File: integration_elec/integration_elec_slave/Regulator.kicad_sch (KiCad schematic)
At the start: 24 parts, among them U4 TPS54335ADDAR

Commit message: EM - fuck it we merge et on cree deux branches
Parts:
- renumbered C36 to C20, C40 to C21, C42 to C22, C44 to C23, C45 to C24, C46 to C25, C60 to C26, C61 to C27, C62 to C28, C63 to C29, C64 to C30, C65 to C31, D9 to D2, L4 to L2, R43 to R14, R44 to R15, R45 to R16, R46 to R17, R47 to R18, R54 to R19, R44 to R20, TP2 to TP1, TP1 to TP2
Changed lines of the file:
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@@
 		(on_board yes)
 		(dnp no)
-		(property "Reference" "R47"
+		(property "Reference" "R18"
 			(at 115.062 44.45 0)
 			(effects
@@
 			(project "integration_elec_slave"
 				(path "/f8f45849-17b1-4cdb-b0ac-47b1208e44f3/408e7880-979e-40de-9541-c2200e8ca76c"
-					(reference "R47")
+					(reference "R18")
 					(unit 1)
 				)
@@
 		(on_board yes)
 		(dnp no)
-		(property "Reference" "C44"
+		(property "Reference" "C23"
 			(at 43.815 34.925 0)
 			(effects
@@
 			(project "integration_elec_slave"
 				(path "/f8f45849-17b1-4cdb-b0ac-47b1208e44f3/408e7880-979e-40de-9541-c2200e8ca76c"
-					(reference "C44")
+					(reference "C23")
 					(unit 1)
 				)
@@
 		(on_board yes)
 		(dnp no)
-		(property "Reference" "D9"
+		(property "Reference" "D2"
 			(at 153.67 47.625 90)
 			(effects
@@
 			(project "integration_elec_slave"
 				(path "/f8f45849-17b1-4cdb-b0ac-47b1208e44f3/408e7880-979e-40de-9541-c2200e8ca76c"
-					(reference "D9")
+					(reference "D2")
 					(unit 1)
 				)
@@
 		(on_board yes)
 		(dnp no)
-		(property "Reference" "TP2"
+		(property "Reference" "TP1"
 			(at 78.5368 69.723 0)
 			(effects
@@
 			(project "integration_elec_slave"
 				(path "/f8f45849-17b1-4cdb-b0ac-47b1208e44f3/408e7880-979e-40de-9541-c2200e8ca76c"
-					(reference "TP2")
+					(reference "TP1")
 					(unit 1)
 				)
@@
 		(on_board yes)
 		(dnp no)
-		(property "Reference" "R45"
+		(property "Reference" "R16"
 			(at 50.165 48.895 0)
 			(effects
@@
 			(project "integration_elec_slave"
 				(path "/f8f45849-17b1-4cdb-b0ac-47b1208e44f3/408e7880-979e-40de-9541-c2200e8ca76c"
-					(reference "R45")
+					(reference "R16")
 					(unit 1)
 				)
@@
 		(on_board yes)
 		(dnp no)
-		(property "Reference" "C36"
+		(property "Reference" "C20"
 			(at 30.48 34.925 0)
 			(effects
@@
 			(project "integration_elec_slave"
 				(path "/f8f45849-17b1-4cdb-b0ac-47b1208e44f3/408e7880-979e-40de-9541-c2200e8ca76c"
-					(reference "C36")
+					(reference "C20")
 					(unit 1)
 				)
@@
 		(on_board yes)
 		(dnp no)
-		(property "Reference" "C63"
+		(property "Reference" "C29"
 			(at 128.27 48.895 0)
 			(effects
@@
 			(project "integration_elec_slave"
 				(path "/f8f45849-17b1-4cdb-b0ac-47b1208e44f3/408e7880-979e-40de-9541-c2200e8ca76c"
-					(reference "C63")
+					(reference "C29")
 					(unit 1)
 				)
@@
 		(dnp no)
 		(fields_autoplaced yes)
-		(property "Reference" "TP1"
+		(property "Reference" "TP2"
 			(at 142.24 30.9879 0)
 			(effects
@@
 			(project ""
 				(path "/f8f45849-17b1-4cdb-b0ac-47b1208e44f3/408e7880-979e-40de-9541-c2200e8ca76c"
-					(reference "TP1")
+					(reference "TP2")
 					(unit 1)
 				)
@@
 		(on_board yes)
 		(dnp no)
-		(property "Reference" "R54"
+		(property "Reference" "R19"
 			(at 115.062 54.61 0)
 			(effects
@@
 			(project "integration_elec_slave"
 				(path "/f8f45849-17b1-4cdb-b0ac-47b1208e44f3/408e7880-979e-40de-9541-c2200e8ca76c"
-					(reference "R54")
+					(reference "R19")
 					(unit 1)
 				)
@@
 		(on_board yes)
 		(dnp no)
-		(property "Reference" "C62"
+		(property "Reference" "C28"
 			(at 121.92 48.895 0)
 			(effects
@@
 			(project "integration_elec_slave"
 				(path "/f8f45849-17b1-4cdb-b0ac-47b1208e44f3/408e7880-979e-40de-9541-c2200e8ca76c"
-					(reference "C62")
+					(reference "C28")
 					(unit 1)
 				)
@@
 		(on_board yes)
 		(dnp no)
-		(property "Reference" "C42"
+		(property "Reference" "C22"
 			(at 39.37 34.925 0)
 			(effects
@@
 			(project "integration_elec_slave"
 				(path "/f8f45849-17b1-4cdb-b0ac-47b1208e44f3/408e7880-979e-40de-9541-c2200e8ca76c"
-					(reference "C42")
+					(reference "C22")
 					(unit 1)
 				)
@@
 		(on_board yes)
 		(dnp no)
-		(property "Reference" "C40"
+		(property "Reference" "C21"
 			(at 34.29 34.925 0)
 			(effects
@@
 			(project "integration_elec_slave"
 				(path "/f8f45849-17b1-4cdb-b0ac-47b1208e44f3/408e7880-979e-40de-9541-c2200e8ca76c"
-					(reference "C40")
+					(reference "C21")
 					(unit 1)
 				)
@@
 		(on_board yes)
 		(dnp no)
-		(property "Reference" "R44"
+		(property "Reference" "R15"
 			(at 43.815 48.895 0)
 			(effects
@@
 			(project "integration_elec_slave"
 				(path "/f8f45849-17b1-4cdb-b0ac-47b1208e44f3/408e7880-979e-40de-9541-c2200e8ca76c"
-					(reference "R44")
+					(reference "R15")
 					(unit 1)
 				)
@@
 		(on_board yes)
 		(dnp no)
-		(property "Reference" "C64"
+		(property "Reference" "C30"
 			(at 134.62 48.895 0)
 			(effects
@@
 			(project "integration_elec_slave"
 				(path "/f8f45849-17b1-4cdb-b0ac-47b1208e44f3/408e7880-979e-40de-9541-c2200e8ca76c"
-					(reference "C64")
+					(reference "C30")
 					(unit 1)
 				)
@@
 		(on_board yes)
 		(dnp no)
-		(property "Reference" "C65"
+		(property "Reference" "C31"
 			(at 141.605 48.895 0)
 			(effects
@@
 			(project "integration_elec_slave"
 				(path "/f8f45849-17b1-4cdb-b0ac-47b1208e44f3/408e7880-979e-40de-9541-c2200e8ca76c"
-					(reference "C65")
+					(reference "C31")
 					(unit 1)
 				)
@@
 		(on_board yes)
 		(dnp no)
-		(property "Reference" "C45"
+		(property "Reference" "C24"
 			(at 48.641 58.801 0)
 			(effects
@@
 			(project "integration_elec_slave"
 				(path "/f8f45849-17b1-4cdb-b0ac-47b1208e44f3/408e7880-979e-40de-9541-c2200e8ca76c"
-					(reference "C45")
+					(reference "C24")
 					(unit 1)
 				)
@@
 		(dnp no)
 		(fields_autoplaced yes)
-		(property "Reference" "L4"
+		(property "Reference" "L2"
 			(at 102.87 36.83 0)
 			(effects
@@
 			(project "integration_elec_slave"
 				(path "/f8f45849-17b1-4cdb-b0ac-47b1208e44f3/408e7880-979e-40de-9541-c2200e8ca76c"
-					(reference "L4")
+					(reference "L2")
 					(unit 1)
 				)
@@
 		(on_board yes)
 		(dnp no)
-		(property "Reference" "C46"
+		(property "Reference" "C25"
 			(at 60.325 55.245 0)
 			(effects
@@
 			(project "integration_elec_slave"
 				(path "/f8f45849-17b1-4cdb-b0ac-47b1208e44f3/408e7880-979e-40de-9541-c2200e8ca76c"
-					(reference "C46")
+					(reference "C25")
 					(unit 1)
 				)
@@
 		(on_board yes)
 		(dnp no)
-		(property "Reference" "R43"
+		(property "Reference" "R14"
 			(at 50.165 39.37 0)
 			(effects
@@
 			(project "integration_elec_slave"
 				(path "/f8f45849-17b1-4cdb-b0ac-47b1208e44f3/408e7880-979e-40de-9541-c2200e8ca76c"
-					(reference "R43")
+					(reference "R14")
 					(unit 1)
 				)
@@
 		(on_board yes)
 		(dnp no)
-		(property "Reference" "#PWR065"
+		(property "Reference" "#PWR029"
 			(at 69.85 71.755 0)
 			(effects
@@
 			(project "integration_elec_slave"
 				(path "/f8f45849-17b1-4cdb-b0ac-47b1208e44f3/408e7880-979e-40de-9541-c2200e8ca76c"
-					(reference "#PWR065")
+					(reference "#PWR029")
 					(unit 1)
 				)
@@
 		(on_board yes)
 		(dnp no)
-		(property "Reference" "R44"
+		(property "Reference" "R20"
 			(at 152.4 57.785 0)
 			(effects
@@
 			(project "integration_elec_slave"
 				(path "/f8f45849-17b1-4cdb-b0ac-47b1208e44f3/408e7880-979e-40de-9541-c2200e8ca76c"
-					(reference "R44")
+					(reference "R20")
 					(unit 1)
 				)
@@
 		(on_board yes)
 		(dnp no)
-		(property "Reference" "C61"
+		(property "Reference" "C27"
 			(at 116.205 48.895 0)
 			(effects
@@
 			(project "integration_elec_slave"
 				(path "/f8f45849-17b1-4cdb-b0ac-47b1208e44f3/408e7880-979e-40de-9541-c2200e8ca76c"
-					(reference "C61")
+					(reference "C27")
 					(unit 1)
 				)
@@
 		(on_board yes)
 		(dnp no)
-		(property "Reference" "R46"
+		(property "Reference" "R17"
 			(at 60.325 50.8 0)
 			(effects
@@
 			(project "integration_elec_slave"
 				(path "/f8f45849-17b1-4cdb-b0ac-47b1208e44f3/408e7880-979e-40de-9541-c2200e8ca76c"
-					(reference "R46")
+					(reference "R17")
 					(unit 1)
 				)
@@
 		(dnp no)
 		(fields_autoplaced yes)
-		(property "Reference" "#PWR019"
+		(property "Reference" "#PWR031"
 			(at 160.02 44.45 0)
 			(effects
@@
 			(project ""
 				(path "/f8f45849-17b1-4cdb-b0ac-47b1208e44f3/408e7880-979e-40de-9541-c2200e8ca76c"
-					(reference "#PWR019")
+					(reference "#PWR031")
 					(unit 1)
 				)
@@
 		(on_board yes)
 		(dnp no)
-		(property "Reference" "#PWR075"
+		(property "Reference" "#PWR030"
 			(at 149.86 70.485 0)
 			(effects
@@
 			(project "integration_elec_slave"
 				(path "/f8f45849-17b1-4cdb-b0ac-47b1208e44f3/408e7880-979e-40de-9541-c2200e8ca76c"
-					(reference "#PWR075")
+					(reference "#PWR030")
 					(unit 1)
 				)
@@
 		(on_board yes)
 		(dnp no)
-		(property "Reference" "C60"
+		(property "Reference" "C26"
 			(at 90.805 33.655 90)
 			(effects
@@
 			(project "integration_elec_slave"
 				(path "/f8f45849-17b1-4cdb-b0ac-47b1208e44f3/408e7880-979e-40de-9541-c2200e8ca76c"
-					(reference "C60")
+					(reference "C26")
 					(unit 1)
 				)
@@
 		(dnp no)
 		(fields_autoplaced yes)
-		(property "Reference" "#PWR020"
+		(property "Reference" "#PWR028"
 			(at 20.32 36.83 0)
 			(effects
@@
 			(project ""
 				(path "/f8f45849-17b1-4cdb-b0ac-47b1208e44f3/408e7880-979e-40de-9541-c2200e8ca76c"
-					(reference "#PWR020")
-					(unit 1)
-				)
+					(reference "#PWR028")
+					(unit 1)
+				)

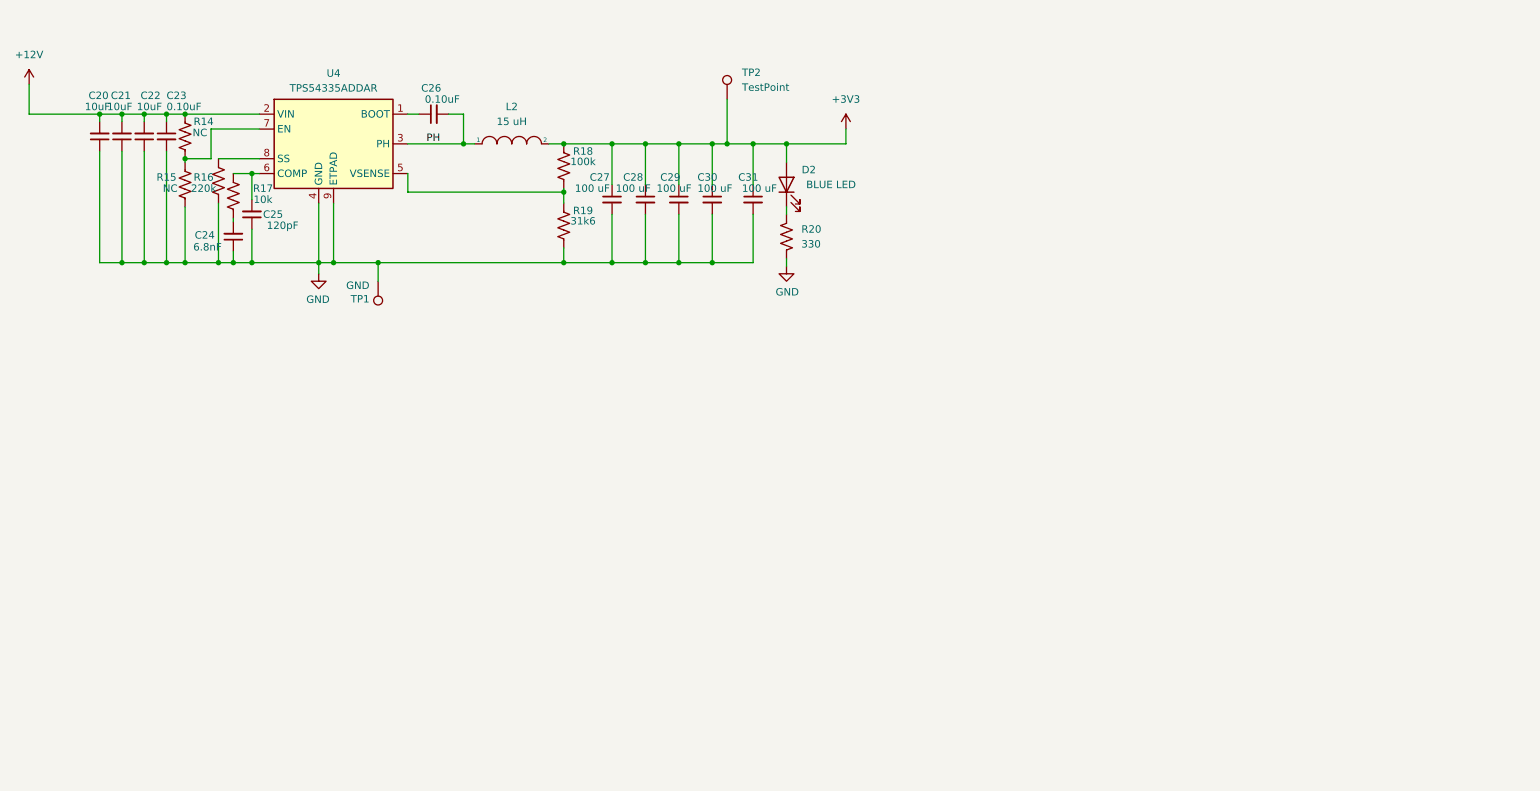
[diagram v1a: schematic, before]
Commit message: EM - Correction des bus
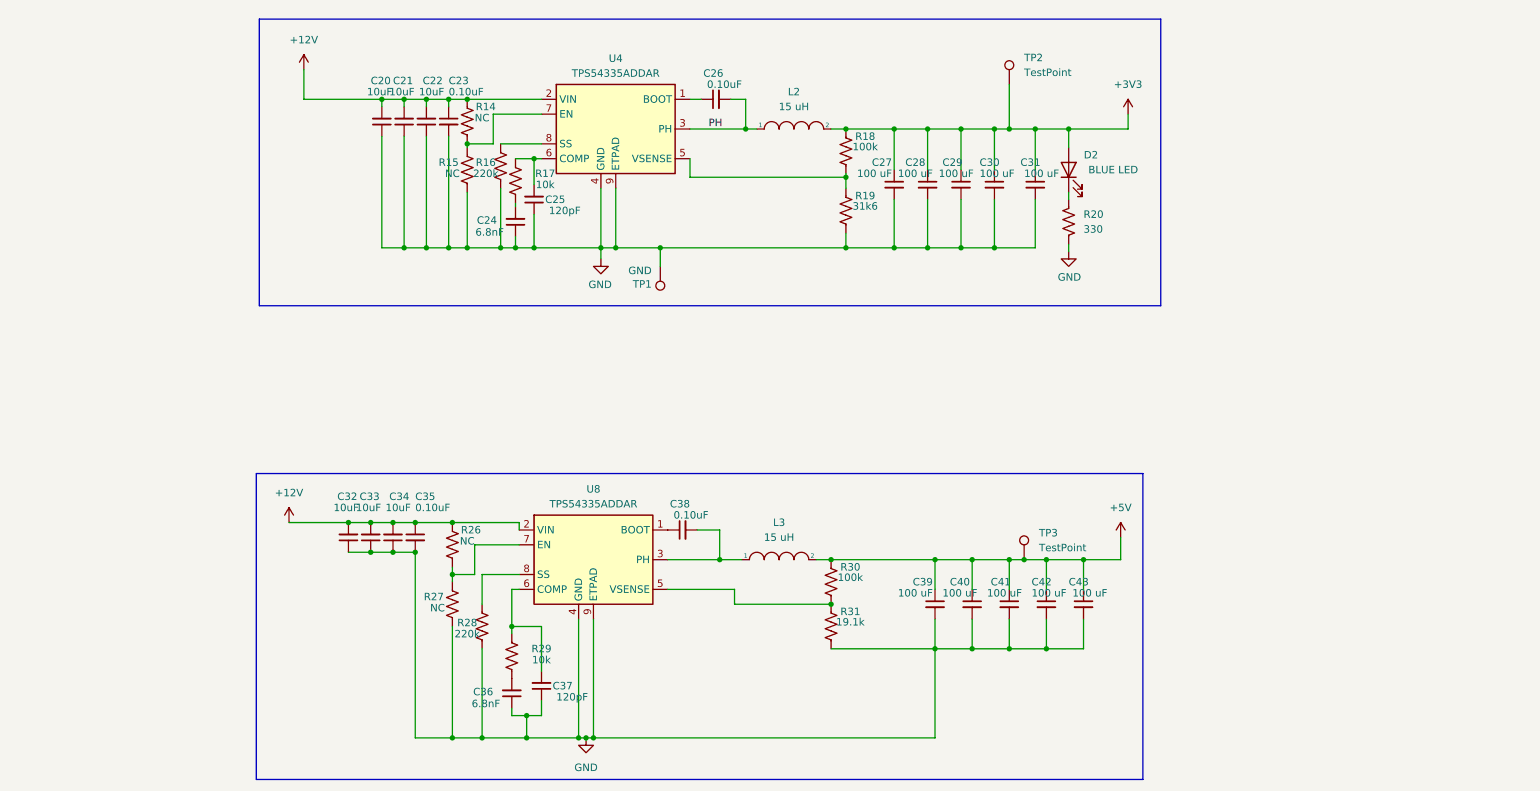
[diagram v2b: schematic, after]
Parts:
- added C32, C33, C34: 10uF, Capacitor_SMD:C_0805_2012Metric_Pad1.18x1.45mm_HandSolder, symbol Device:C_Small
- added C35, C38: 0.10uF, Capacitor_SMD:C_0805_2012Metric_Pad1.18x1.45mm_HandSolder, symbol Device:C_Small
- added C36: 6.8nF, Capacitor_SMD:C_0805_2012Metric_Pad1.18x1.45mm_HandSolder, symbol Device:C_Small
- added C37: 120pF, Capacitor_SMD:C_0805_2012Metric_Pad1.18x1.45mm_HandSolder, symbol Device:C_Small
- added C39, C40, C41, C42, C43: 100 uF, Capacitor_SMD:C_1206_3216Metric, symbol Device:C_Small
- added L3: 15 uH, Inductors:IND_BOURNS_SRR1280, symbol pspice:INDUCTOR
- added R26, R27: NC, Resistor_SMD:R_0805_2012Metric_Pad1.20x1.40mm_HandSolder, symbol Device:R_US
- added R28: 220k, Resistor_SMD:R_0805_2012Metric_Pad1.20x1.40mm_HandSolder, symbol Device:R_US
- added R29: 10k, Resistor_SMD:R_0805_2012Metric_Pad1.20x1.40mm_HandSolder, symbol Device:R_US
- added R30: 100k, Resistor_SMD:R_0805_2012Metric_Pad1.20x1.40mm_HandSolder, symbol Device:R_US
- added R31: 19.1k, Resistor_SMD:R_0805_2012Metric_Pad1.20x1.40mm_HandSolder, symbol Device:R_US
- added TP3: TestPoint, symbol Connector:TestPoint
- added U8: TPS54335ADDAR, Package_SO:TI_SO-PowerPAD-8_ThermalVias, symbol Regulator_Switching:TPS54336ADDA
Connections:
- net +12V: now also C32.2, C33.2, C34.2, C35.1, R26.1, U8.2 (VIN)
- net GND: now also C32.1, C33.1, C34.1, C35.2, C36.1, C37.1, C39.2, C40.2, C41.2, C42.2, C43.2, R27.2, R28.2, R31.2, U8.4 (GND), U8.9 (ETPAD)
- new net: R26.2, R27.1, U8.7 (EN)
- new net: R28.1, U8.8 (SS)
- new net: C38.2, L3.1, U8.3 (PH)
- new net: C37.2, R29.1, U8.6 (COMP)
- new net: C36.2, R29.2
- new net: C38.1, U8.1 (BOOT)
- new net: R30.2, R31.1, U8.5 (VSENSE)
- new net +5V: C39.1, C40.1, C41.1, C42.1, C43.1, L3.2, R30.1, TP3.1
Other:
- moved on the sheet: C20, C21, C22, C23, C24, C25, C26, C27, C28, C29, C30, C31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

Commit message: EM - Fini schématique attente de review
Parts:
- R31: DigiKey (none) -> 311-19.1KCRCT-ND
- TP2, TP3: footprint (none) -> TestPoint:TestPoint_Plated_Hole_D2.0mm
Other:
- moved on the sheet: C24, R16

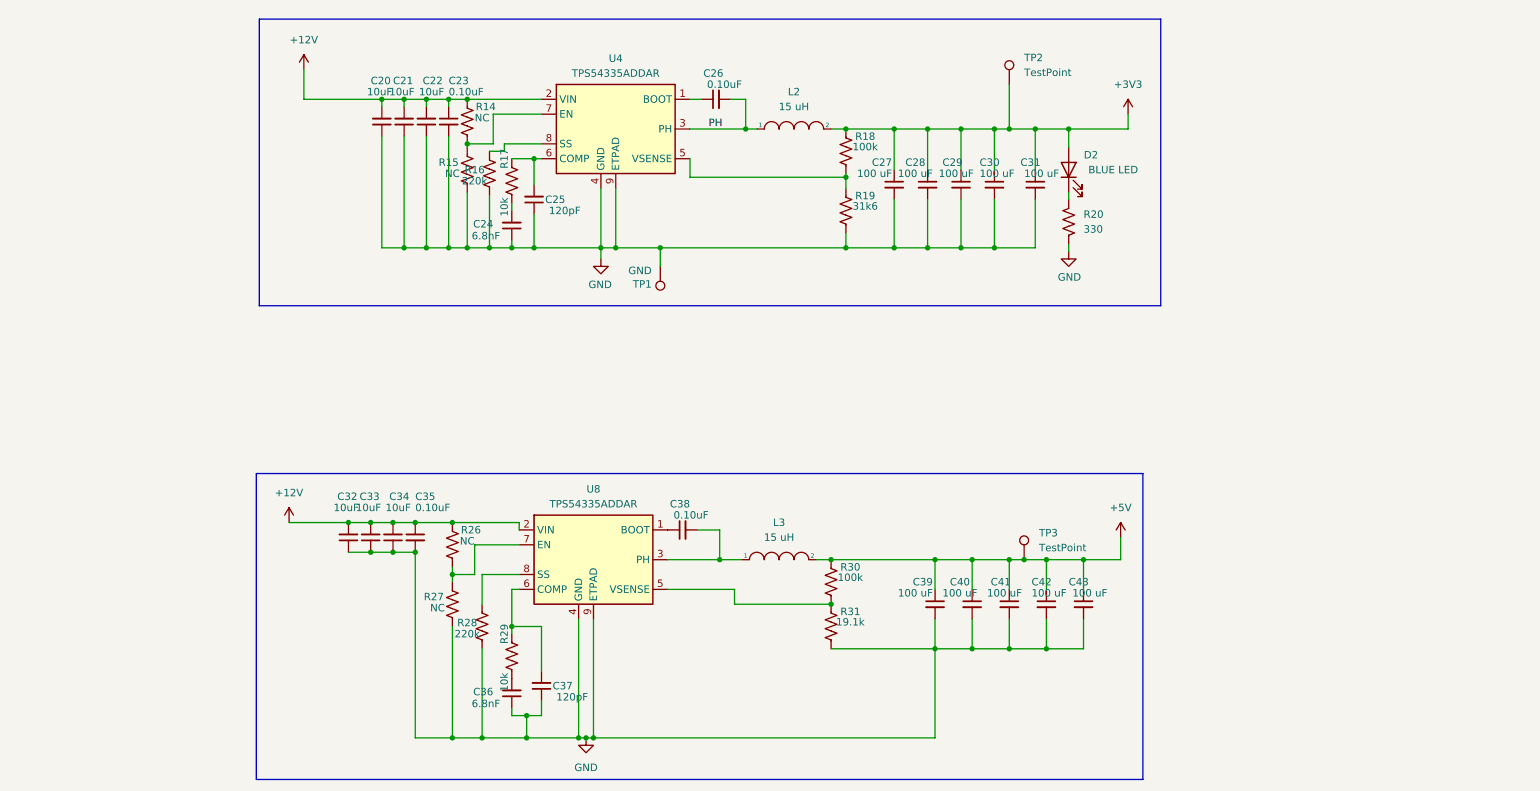
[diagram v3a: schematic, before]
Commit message: EM - Fin du schématique, ajout de diode pour empêcher de backfeeder le USB. Début PCB et ajout carré 100x100
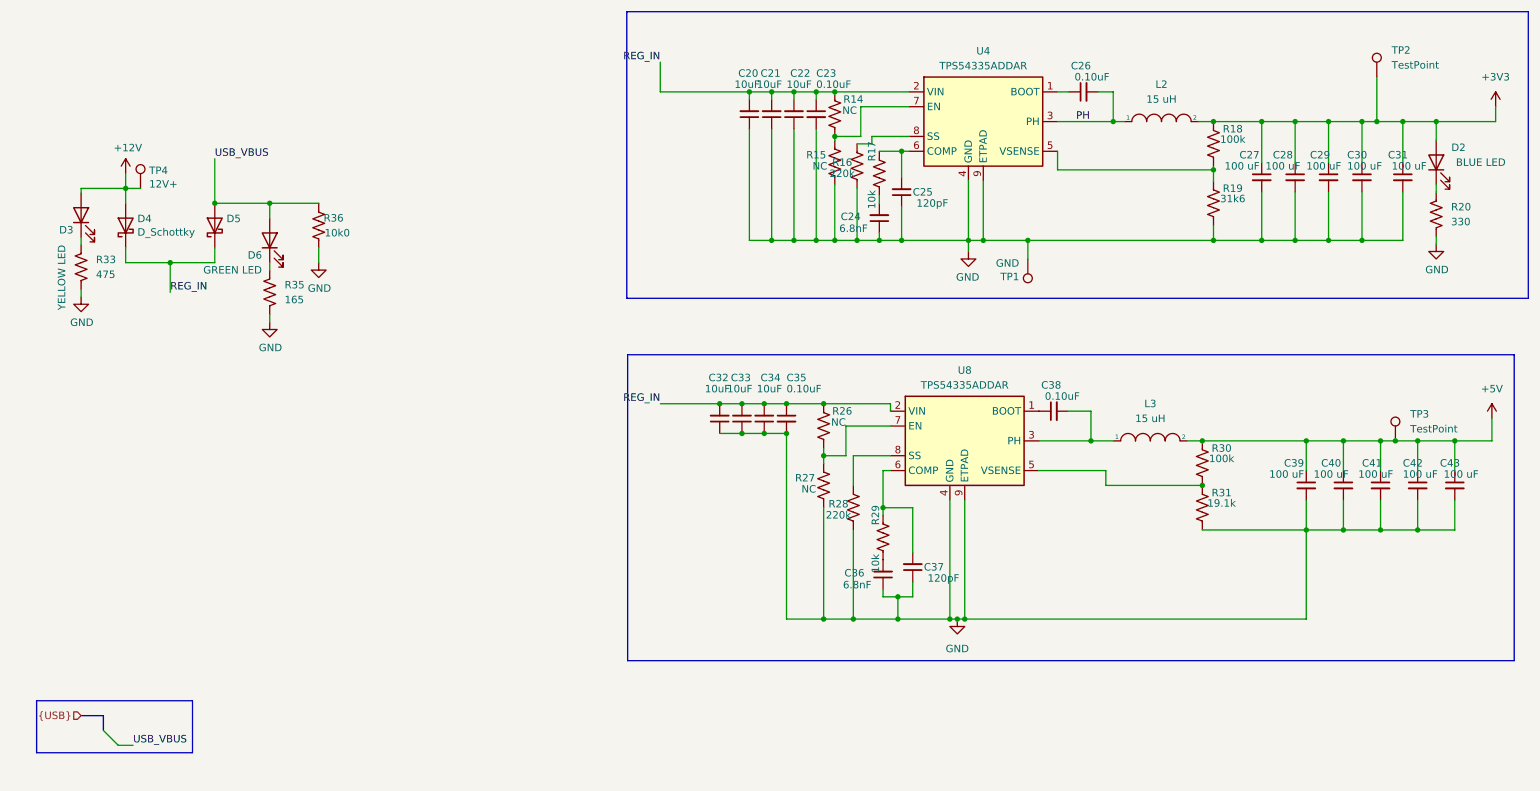
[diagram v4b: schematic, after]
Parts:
- added D3: YELLOW LED, LED_SMD:LED_1206_3216Metric, symbol Device:LED
- added D4, D5: D_Schottky, SCHTKY_DIODE:SOD323-HE, symbol Device:D_Schottky
- added D6: GREEN LED, LED_SMD:LED_1206_3216Metric, symbol Device:LED
- added R33: 475, Resistor_SMD:R_0805_2012Metric_Pad1.20x1.40mm_HandSolder, symbol Device:R_US
- added R35: 165, Resistor_SMD:R_0805_2012Metric_Pad1.20x1.40mm_HandSolder, symbol Device:R_US
- added R36: 10k0, Resistor_SMD:R_0603_1608Metric_Pad0.98x0.95mm_HandSolder, symbol Device:R_US
- added TP4: 12V+, TestPoint:TestPoint_Plated_Hole_D2.0mm, symbol Connector:TestPoint
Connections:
- net +12V: now also D3.2 (A), D4.2 (A), TP4.1; no longer C20.2, C21.2, C22.2, C23.1, C32.2, C33.2, C34.2, C35.1, R14.1, R26.1, U4.2 (VIN), U8.2 (VIN)
- net GND: now also R33.2, R35.2, R36.2
- new net: D3.1 (K), R33.1
- new net: D6.1 (K), R35.1
- new net REG_IN: C20.2, C21.2, C22.2, C23.1, C32.2, C33.2, C34.2, C35.1, D4.1 (K), D5.1 (K), R14.1, R26.1, U4.2 (VIN), U8.2 (VIN)
- new net USB_VBUS: D5.2 (A), D6.2 (A), R36.1
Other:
- moved on the sheet: C20, C21, C22, C23, C24, C25, C26, C27, C28, C29, C30, C31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
